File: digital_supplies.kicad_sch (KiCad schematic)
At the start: 56 parts, among them Q1 PMOS, Q2 2PNP, Q8 PMOS, U19 74LVC1G06, U4 3V3REG, U5 LDO-ADJ, U6 LDO-ADJ, U7 LDO-ADJ

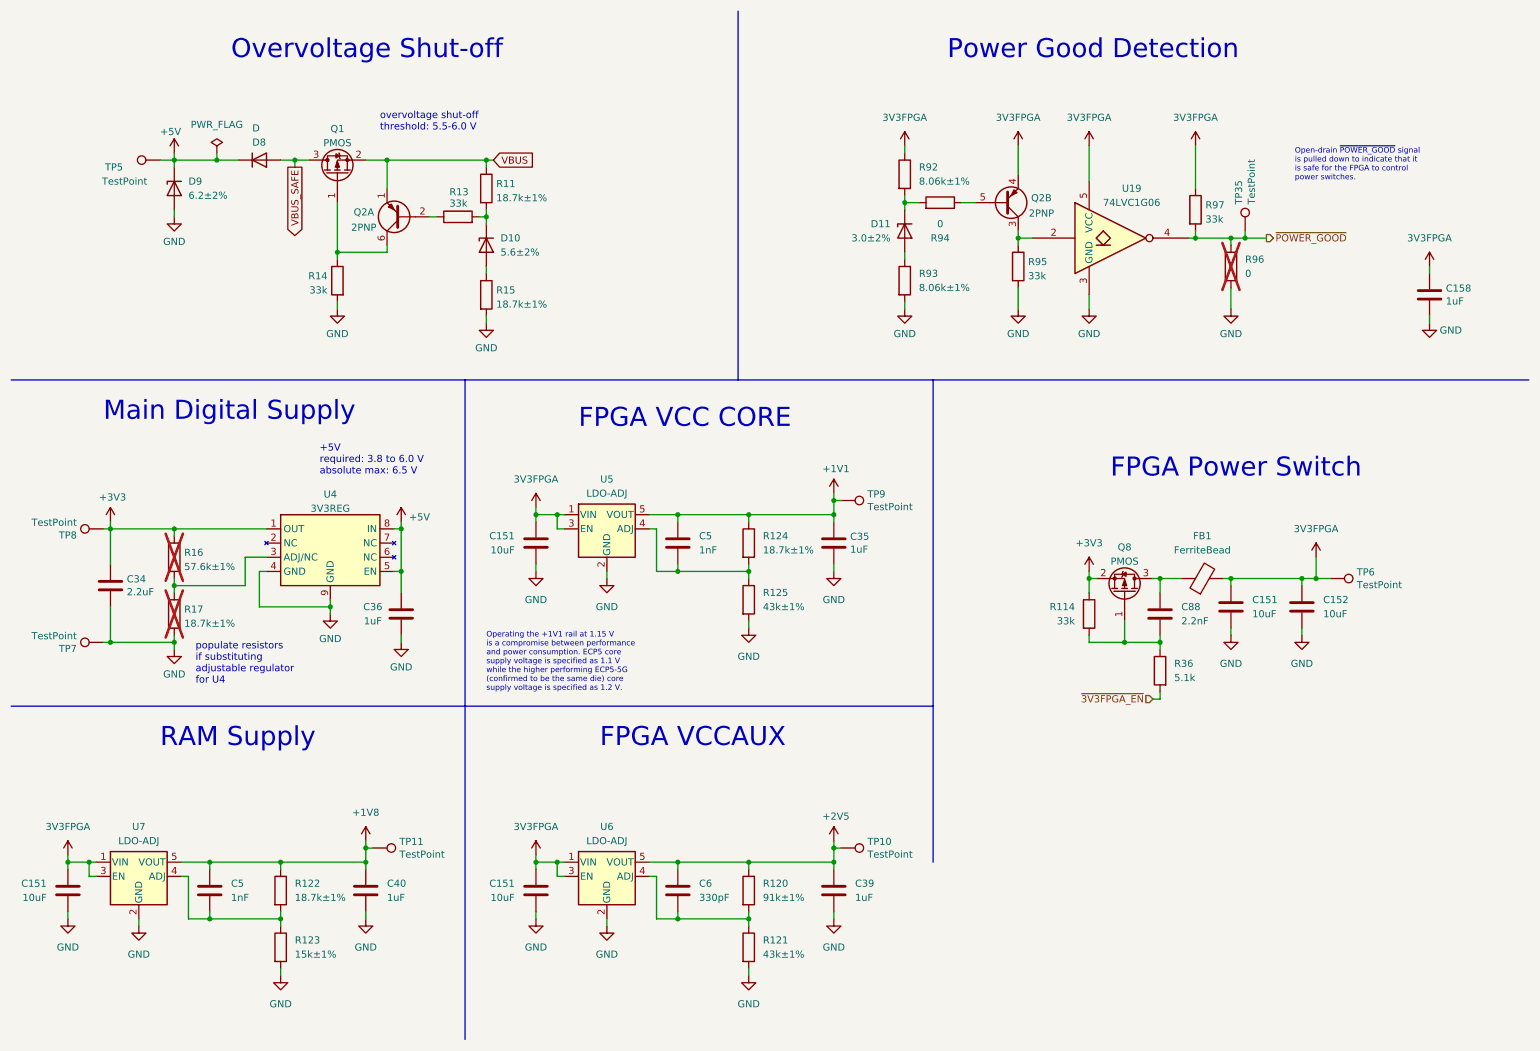
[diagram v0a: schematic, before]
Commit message: Replace open drain clock inverters with push-pull
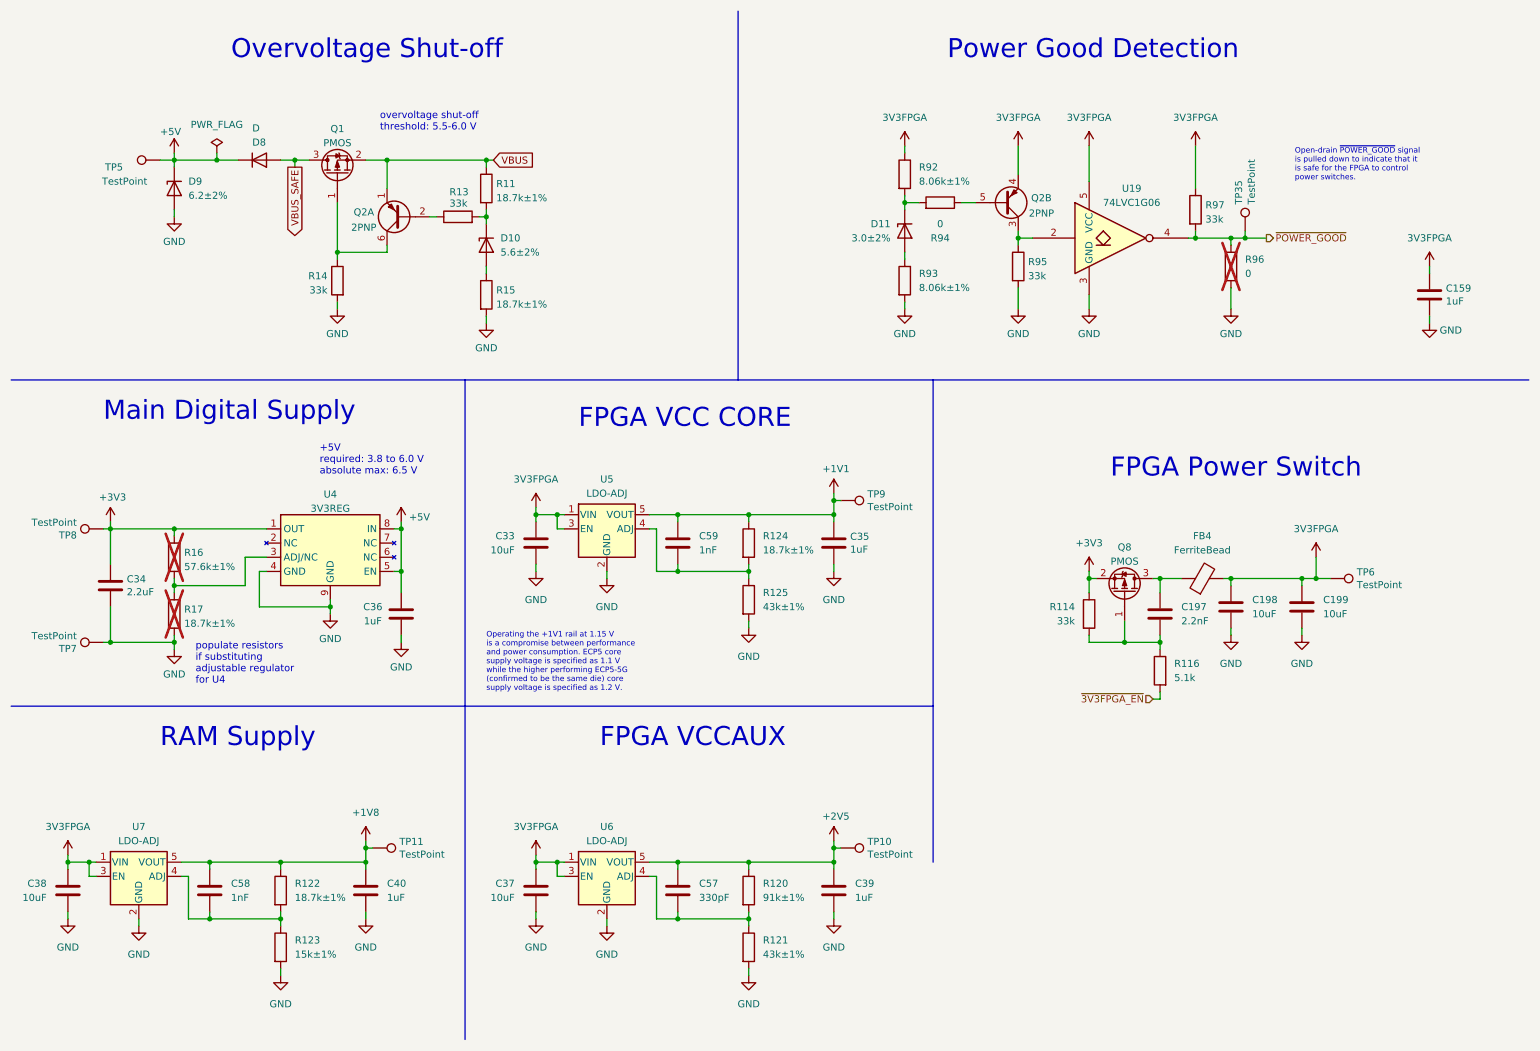
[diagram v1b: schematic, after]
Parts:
- renumbered C158 to C159, C88 to C197, C151 to C198, C152 to C199, C151 to C33, C151 to C37, C151 to C38, C6 to C57, C5 to C58, C5 to C59, FB1 to FB4, R36 to R116

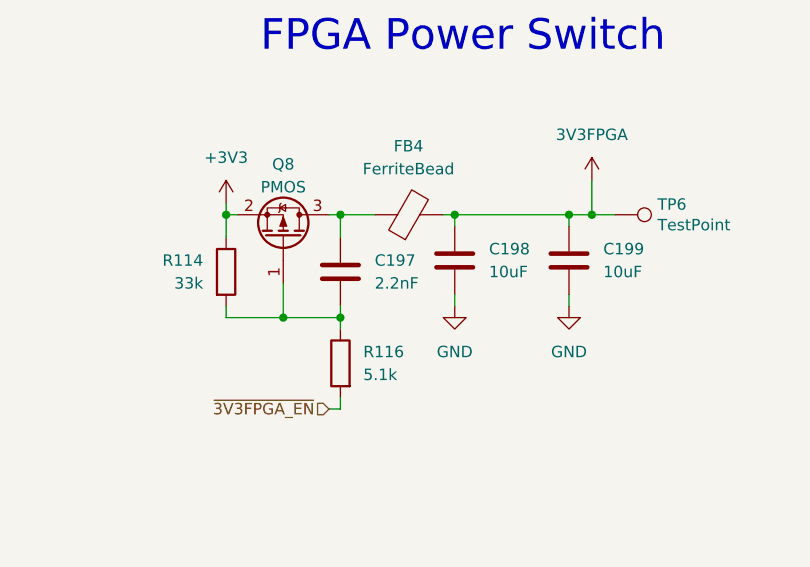
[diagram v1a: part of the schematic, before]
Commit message: Tune slow-start capacitors
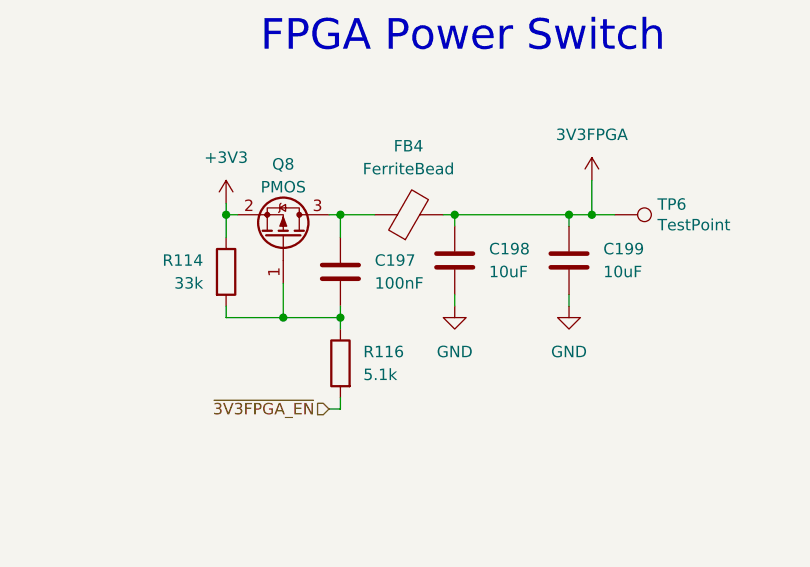
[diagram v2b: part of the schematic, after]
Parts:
- C197: value 2.2nF -> 100nF; Part Number GRM033R71A222KA01D -> GRM033R61A104KE15D; Substitution GRM033R71A222KA01* -> GRM033R61A104KE15*
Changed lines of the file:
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@@
       (effects (font (size 1.27 1.27)) (justify right))
     )
-    (property "Value" "2.2nF" (at 222.25 121.92 0)
+    (property "Value" "100nF" (at 222.25 121.92 0)
       (effects (font (size 1.27 1.27)) (justify right))
     )
@@
       (effects (font (size 1.27 1.27)) hide)
     )
-    (property "Description" "CAP CER 2200PF 10V X7R 0201" (at 218.44 120.65 0)
+    (property "Description" "CAP CER 0.1UF 10V X5R 0201" (at 218.44 120.65 0)
       (effects (font (size 1.27 1.27)) hide)
     )
@@
       (effects (font (size 1.27 1.27)) hide)
     )
-    (property "Part Number" "GRM033R71A222KA01D" (at 218.44 120.65 0)
+    (property "Part Number" "GRM033R61A104KE15D" (at 218.44 120.65 0)
       (effects (font (size 1.27 1.27)) hide)
     )
-    (property "Substitution" "GRM033R71A222KA01*" (at 218.44 120.65 0)
+    (property "Substitution" "GRM033R61A104KE15*" (at 218.44 120.65 0)
       (effects (font (size 1.27 1.27)) hide)
     )
